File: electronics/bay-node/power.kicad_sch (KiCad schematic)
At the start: 23 parts, among them J1 ROW IN, J2 ROW OUT, Q1 SUD50P06-15(UMW), U1 LMR51625YDDCR, U2 AP2114H-3.3TRG1

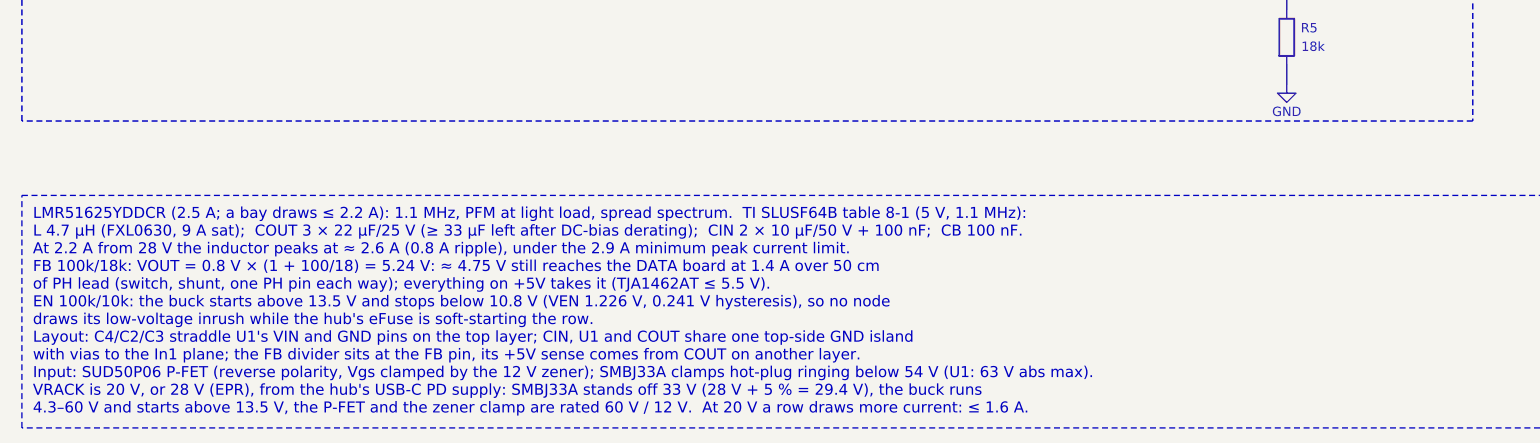
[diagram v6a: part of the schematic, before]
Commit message: Schematic review S1, S4, S6: POS_IN 150k, the hub's ON LEDs on 18k, the camera's 0.75 A PTC
The user approved them ("S1 oui / S6 oui / S4 oui").

* S1, bay node: R29 470k -> 150k (C22807, basic).
  - Before its firmware runs, the upstream POS output (a node's IO42, the
    hub's IO10-13) floats. The BAT54S's warm leakage (about 2-3 uA at
    65 C) could then lift POS_IN through 470k to VIL.
  - Driven high through R30 + R28, 150k still gives 2.87 V, above VIH.
  - The design.py notes and bay_node.dtsi follow.
* S4, power hub: R41-R44 (the ON LEDs on the row outputs) 10k -> 18k
  (C25810, already on the board): 1.4 mA and 37 mW at 28 V. The 10k
  ran at 75 % of its 0603 rating at 29.4 V.
* S6, bay node: F1 (CAM_5V) goes from the 0.5 A PTC to SMD1206P075TF
  (RUILON, C20987, new catalog key pptc750): 0.75 A hold, 1.5 A trip,
  the same 1206 footprint. It is extended like C20799, so no fee changes.
  - Arducam gives the Mega 317 mA working: with the LEDs that is
    ~0.42 A on CAM_5V, where the 0.5 A part holds ~0.31 A at 70 C.
  - The camera pod's LDO tab gets the copper its routing leaves: a
    top-side +3V3 pour round the tab and a bottom-side island, joined by
    three vias. U1 drops ~0.5 W at 317 mA. The routing is unchanged.
  - The "~120 mA" notes go to 317 mA (node and pod design.py,
    electronics.md).
  - The bay's worst case follows: <= 2.25 A on +5V, the buck's inductor
    peaking at ~2.65 A (under its 2.9 A minimum limit), 13.5 W from
    VRACK (power-distribution-review.md, the buck notes).

The routed PCBs keep their routing.
- Node and hub: only the changed parts' properties (KiCad's Python, as
  pcbgen sets them).
- Pod: the two new zones and three vias, refilled.
- ERC 0, DRC 0, unconnected 0, parity 0 on all three (run on the Mac:
  zephyrbox didn't answer).
- keep_unchanged kept the node's renders and the hub's Gerbers. The
  hub's bottom render is restored: 9 pixels of via-hole noise, as before.
- The pod's renders, Gerbers and viewer GLB chang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
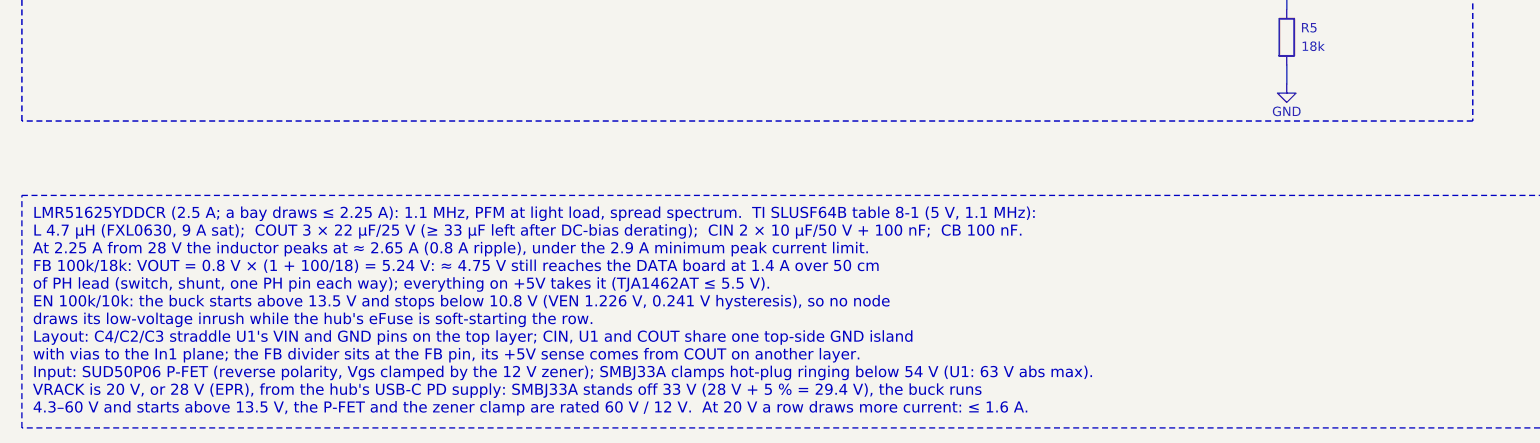
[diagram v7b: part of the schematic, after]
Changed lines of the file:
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@@
 		)
 	)
-	(text_box "LMR51625YDDCR (2.5 A; a bay draws ≤ 2.2 A): 1.1 MHz, PFM at light load, spread spectrum.  TI SLUSF64B table 8-1 (5 V, 1.1 MHz):\n  L 4.7 µH (FXL0630, 9 A sat);  COUT 3 × 22 µF/25 V (≥ 33 µF left after DC-bias derating);  CIN 2 × 10 µF/50 V + 100 nF;  CB 100 nF.\n  At 2.2 A from 28 V the inductor peaks at ≈ 2.6 A (0.8 A ripple), under the 2.9 A minimum peak current limit.\nFB 100k/18k: VOUT = 0.8 V × (1 + 100/18) = 5.24 V: ≈ 4.75 V still reaches the DATA board at 1.4 A over 50 cm\n  of PH lead (switch, shunt, one PH pin each way); everything on +5V takes it (TJA1462AT ≤ 5.5 V).\nEN 100k/10k: the buck starts above 13.5 V and stops below 10.8 V (VEN 1.226 V, 0.241 V hysteresis), so no node\n  draws its low-voltage inrush while the hub's eFuse is soft-starting the row.\nLayout: C4/C2/C3 straddle U1's VIN and GND pins on the top layer; CIN, U1 and COUT share one top-side GND island\n  with vias to the In1 plane; the FB divider sits at the FB pin, its +5V sense comes from COUT on another layer.\nInput: SUD50P06 P-FET (reverse polarity, Vgs clamped by the 12 V zener); SMBJ33A clamps hot-plug ringing below 54 V (U1: 63 V abs max).\nVRACK is 20 V, or 28 V (EPR), from the hub's USB-C PD supply: SMBJ33A stands off 33 V (28 V + 5 % = 29.4 V), the buck runs\n  4.3–60 V and starts above 13.5 V, the P-FET and the zener clamp are rated 60 V / 12 V.  At 20 V a row draws more current: ≤ 1.6 A."
+	(text_box "LMR51625YDDCR (2.5 A; a bay draws ≤ 2.25 A): 1.1 MHz, PFM at light load, spread spectrum.  TI SLUSF64B table 8-1 (5 V, 1.1 MHz):\n  L 4.7 µH (FXL0630, 9 A sat);  COUT 3 × 22 µF/25 V (≥ 33 µF left after DC-bias derating);  CIN 2 × 10 µF/50 V + 100 nF;  CB 100 nF.\n  At 2.25 A from 28 V the inductor peaks at ≈ 2.65 A (0.8 A ripple), under the 2.9 A minimum peak current limit.\nFB 100k/18k: VOUT = 0.8 V × (1 + 100/18) = 5.24 V: ≈ 4.75 V still reaches the DATA board at 1.4 A over 50 cm\n  of PH lead (switch, shunt, one PH pin each way); everything on +5V takes it (TJA1462AT ≤ 5.5 V).\nEN 100k/10k: the buck starts above 13.5 V and stops below 10.8 V (VEN 1.226 V, 0.241 V hysteresis), so no node\n  draws its low-voltage inrush while the hub's eFuse is soft-starting the row.\nLayout: C4/C2/C3 straddle U1's VIN and GND pins on the top layer; CIN, U1 and COUT share one top-side GND island\n  with vias to the In1 plane; the FB divider sits at the FB pin, its +5V sense comes from COUT on another layer.\nInput: SUD50P06 P-FET (reverse polarity, Vgs clamped by the 12 V zener); SMBJ33A clamps hot-plug ringing below 54 V (U1: 63 V abs max).\nVRACK is 20 V, or 28 V (EPR), from the hub's USB-C PD supply: SMBJ33A stands off 33 V (28 V + 5 % = 29.4 V), the buck runs\n  4.3–60 V and starts above 13.5 V, the P-FET and the zener clamp are rated 60 V / 12 V.  At 20 V a row draws more current: ≤ 1.6 A."
 		(exclude_from_sim no)
 		(at 15.24 162.56 0)

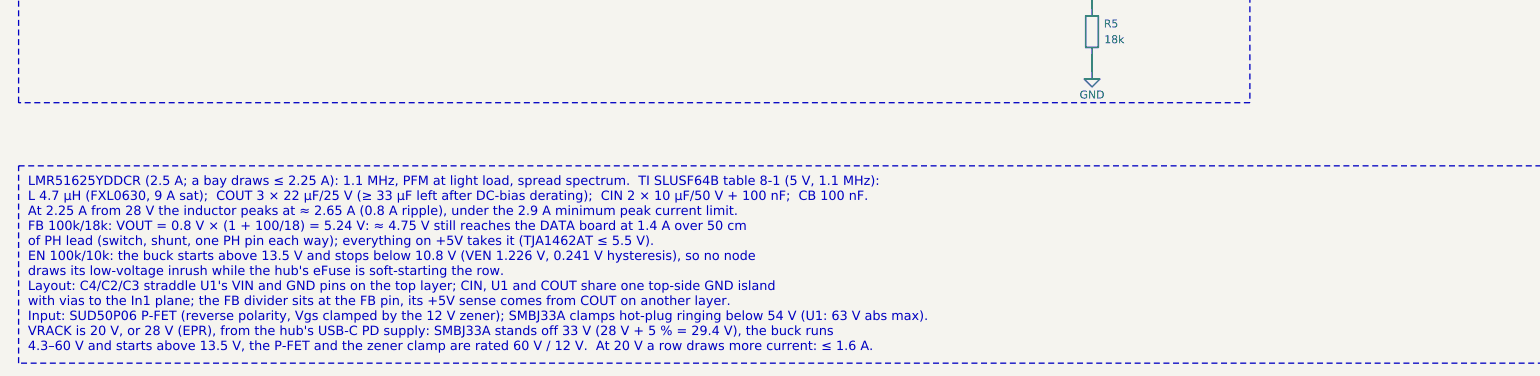
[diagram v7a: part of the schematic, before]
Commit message: Datasheet audit F1-F6: the pod's AP2114H, STB 5.1k, PC_DET hysteresis, the camera ESD's 100 nF, the eFuse step
The user approved the audit's fixes for the node, the hub and the pod
("Go pour 1"); docs/datasheet-audit.md marks F1-F6 applied.

* F1, camera pod: U1 AMS1117-3.3 -> AP2114H-3.3TRG1 (C150716, catalog
  ldo_1a, the node's U2).
  - The AMS1117 is specified stable only with 22 uF tantalum; the
    AP2114H is stable with the ceramic C2.
  - Same SOT-223 pinout, copper (the +3V3 pour and island round the
    tab stay) and 180 deg CPL correction.
  - One more extended type on the pod's Economic order: +$3.09 and
    $0.05 of parts (JLC_SINCE_QUOTE).
* F2, power hub: R214 (TJA1462 STB pull-down) 10k -> 5.1k (C23186,
  already on the board). With IO9 floating, STB's internal pull-up
  (20 kOhm minimum) left it at up to 1.10 V, over VIL 0.99 V.
* F3, bay node: R42 150k from MUX_SEL back to PC_DET, beside U7 (C22807,
  on the board since S1).
  - The laptop's VBUS rises at ~50 us/V through R11/R12, where the
    LVC1G32 wants <= 10 ns/V and warns of oscillation.
  - This gives ~0.14 V of hysteresis.
* F4, bay node: C28 100 nF (C14663) on U12/U13's VBUS pins (+3V3), above
  U12 by its pin 5. Between the two ICs their courtyards leave no room.
* F5, node and hub: firmware.md's first-flash procedure gains the
  irreversible DIS_USB_OTG_DOWNLOAD_MODE eFuse step. In USB-OTG
  download boot the ROM drives IO40 high: the node's DUT_FLT_N, the
  hub's PD_SCL. Nothing is burnt.
* F6, notes, hub:
  - the IMON filter is 0.9 ms, not 47 us: the pin is a current source;
  - the buck stops at ~3.8 V (internal UVLO);
  - SHDN turns on at >= 1 V;
  - the soft start stays under the limit only typically;
  - the CH224A note follows CH224 V2.1: the source PDOs are listed for
    both parts and readable under 100 W, which is still to check with
    ours (review R3); single-byte transfers; no "same die".
* F6, notes, node: TPS2553D; the LDO's 1.94 V x 0.4 A ~ 0.8 W; L1's
  7.5 A guarante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
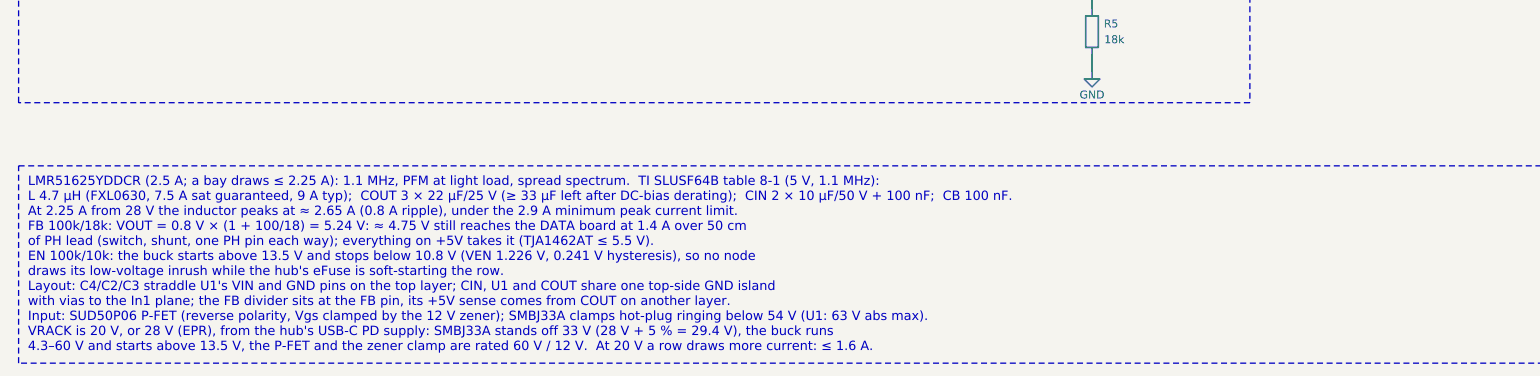
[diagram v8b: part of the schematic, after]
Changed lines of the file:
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@@
 		(comment 1 "ESP32-S3 USB/IP host for one bay of the hw-testing-rack shelf")
 		(comment 2 "Generated from electronics/bay-node/design.py — edit the Python, then regenerate")
-		(comment 3 "Row bus 20–28 V + CAN + POS in/out · 5 V/1.4 A switched DUT port · USB 2.0 muxes · INA226 · AUX")
+		(comment 3 "Row bus 20–28 V + CAN + POS in/out · 5 V/1.4 A switched DUT power on the DATA lead · USB 2.0 muxes · INA226 · AUX")
 	)
 	(symbol
@@
 			)
 		)
-		(property "Description" "4.7 µH, 9 A sat, 6 A rms, 33 mΩ, molded"
+		(property "Description" "4.7 µH, 7.5 A sat (9 A typ), 5.5 A rms, 33 mΩ, molded"
 			(at 146.05 116.84 0)
 			(effects
@@
 		)
 	)
-	(text_box "LMR51625YDDCR (2.5 A; a bay draws ≤ 2.25 A): 1.1 MHz, PFM at light load, spread spectrum.  TI SLUSF64B table 8-1 (5 V, 1.1 MHz):\n  L 4.7 µH (FXL0630, 9 A sat);  COUT 3 × 22 µF/25 V (≥ 33 µF left after DC-bias derating);  CIN 2 × 10 µF/50 V + 100 nF;  CB 100 nF.\n  At 2.25 A from 28 V the inductor peaks at ≈ 2.65 A (0.8 A ripple), under the 2.9 A minimum peak current limit.\nFB 100k/18k: VOUT = 0.8 V × (1 + 100/18) = 5.24 V: ≈ 4.75 V still reaches the DATA board at 1.4 A over 50 cm\n  of PH lead (switch, shunt, one PH pin each way); everything on +5V takes it (TJA1462AT ≤ 5.5 V).\nEN 100k/10k: the buck starts above 13.5 V and stops below 10.8 V (VEN 1.226 V, 0.241 V hysteresis), so no node\n  draws its low-voltage inrush while the hub's eFuse is soft-starting the row.\nLayout: C4/C2/C3 straddle U1's VIN and GND pins on the top layer; CIN, U1 and COUT share one top-side GND island\n  with vias to the In1 plane; the FB divider sits at the FB pin, its +5V sense comes from COUT on another layer.\nInput: SUD50P06 P-FET (reverse polarity, Vgs clamped by the 12 V zener); SMBJ33A clamps hot-plug ringing below 54 V (U1: 63 V abs max).\nVRACK is 20 V, or 28 V (EPR), from the hub's USB-C PD supply: SMBJ33A stands off 33 V (28 V + 5 % = 29.4 V), the buck runs\n  4.3–60 V and starts above 13.5 V, the P-FET and the zener clamp are rated 60 V / 12 V.  At 20 V a row draws more current: ≤ 1.6 A."
+	(text_box "LMR51625YDDCR (2.5 A; a bay draws ≤ 2.25 A): 1.1 MHz, PFM at light load, spread spectrum.  TI SLUSF64B table 8-1 (5 V, 1.1 MHz):\n  L 4.7 µH (FXL0630, 7.5 A sat guaranteed, 9 A typ);  COUT 3 × 22 µF/25 V (≥ 33 µF left after DC-bias derating);  CIN 2 × 10 µF/50 V + 100 nF;  CB 100 nF.\n  At 2.25 A from 28 V the inductor peaks at ≈ 2.65 A (0.8 A ripple), under the 2.9 A minimum peak current limit.\nFB 100k/18k: VOUT = 0.8 V × (1 + 100/18) = 5.24 V: ≈ 4.75 V still reaches the DATA board at 1.4 A over 50 cm\n  of PH lead (switch, shunt, one PH pin each way); everything on +5V takes it (TJA1462AT ≤ 5.5 V).\nEN 100k/10k: the buck starts above 13.5 V and stops below 10.8 V (VEN 1.226 V, 0.241 V hysteresis), so no node\n  draws its low-voltage inrush while the hub's eFuse is soft-starting the row.\nLayout: C4/C2/C3 straddle U1's VIN and GND pins on the top layer; CIN, U1 and COUT share one top-side GND island\n  with vias to the In1 plane; the FB divider sits at the FB pin, its +5V sense comes from COUT on another layer.\nInput: SUD50P06 P-FET (reverse polarity, Vgs clamped by the 12 V zener); SMBJ33A clamps hot-plug ringing below 54 V (U1: 63 V abs max).\nVRACK is 20 V, or 28 V (EPR), from the hub's USB-C PD supply: SMBJ33A stands off 33 V (28 V + 5 % = 29.4 V), the buck runs\n  4.3–60 V and starts above 13.5 V, the P-FET and the zener clamp are rated 60 V / 12 V.  At 20 V a row draws more current: ≤ 1.6 A."
 		(exclude_from_sim no)
 		(at 15.24 162.56 0)
